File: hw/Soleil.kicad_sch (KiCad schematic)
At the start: 43 parts, among them J1 Conn_01x04, Q1 2N7002, SW1 SW_Push, U1 SPV1040TTR, U2 TPS61220DCK, U3 STM32G030F6Px, U4 ZJY200200-0154DAAMFGN

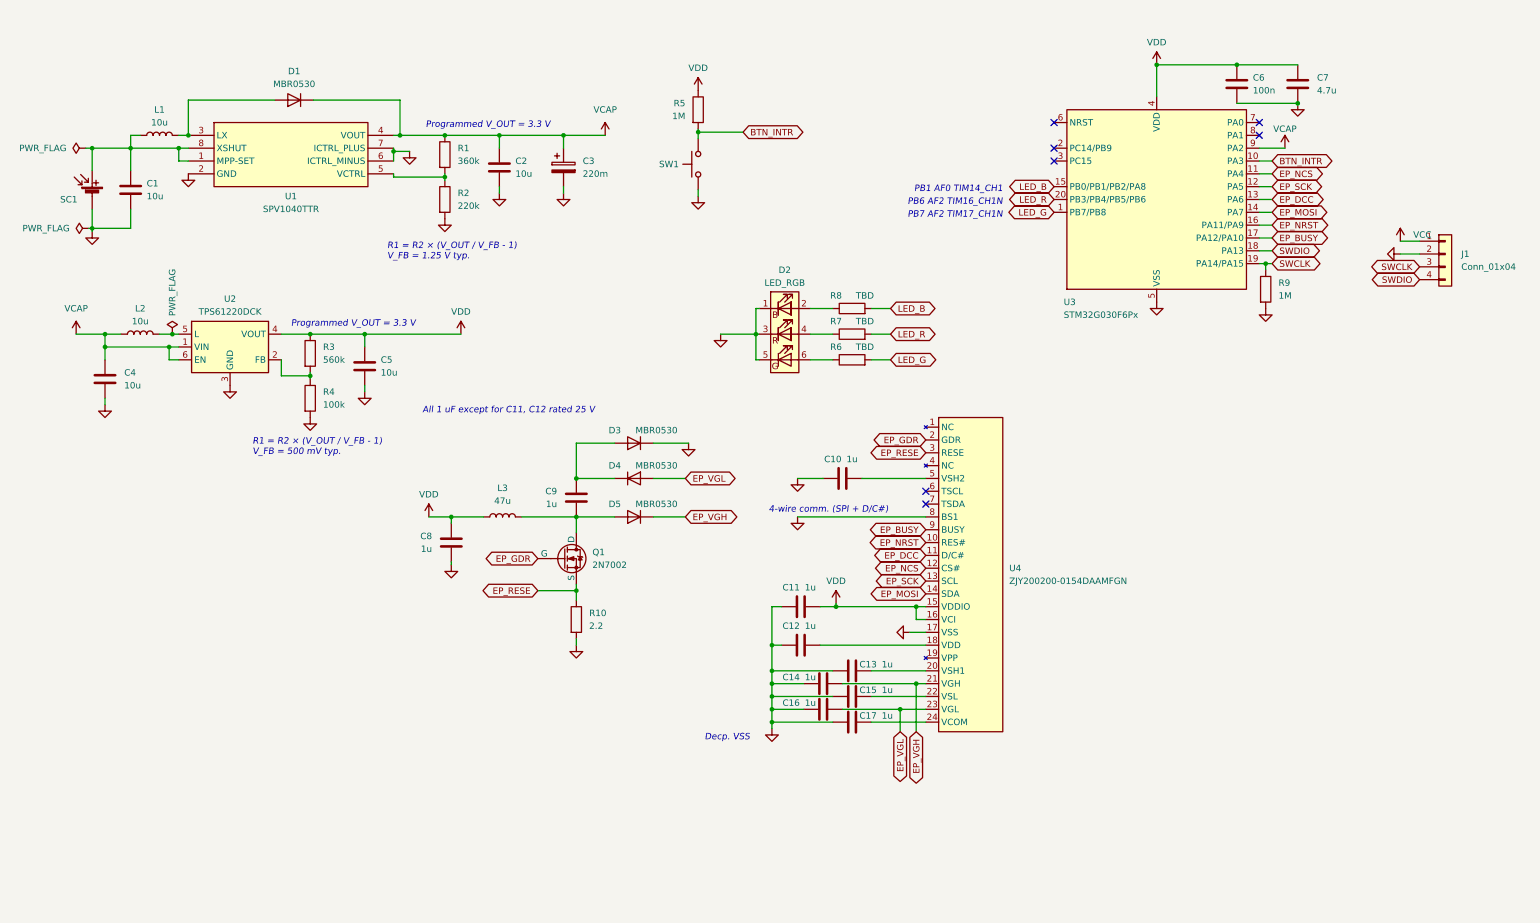
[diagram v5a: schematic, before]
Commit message: Update schematic to include analogue switch and flash
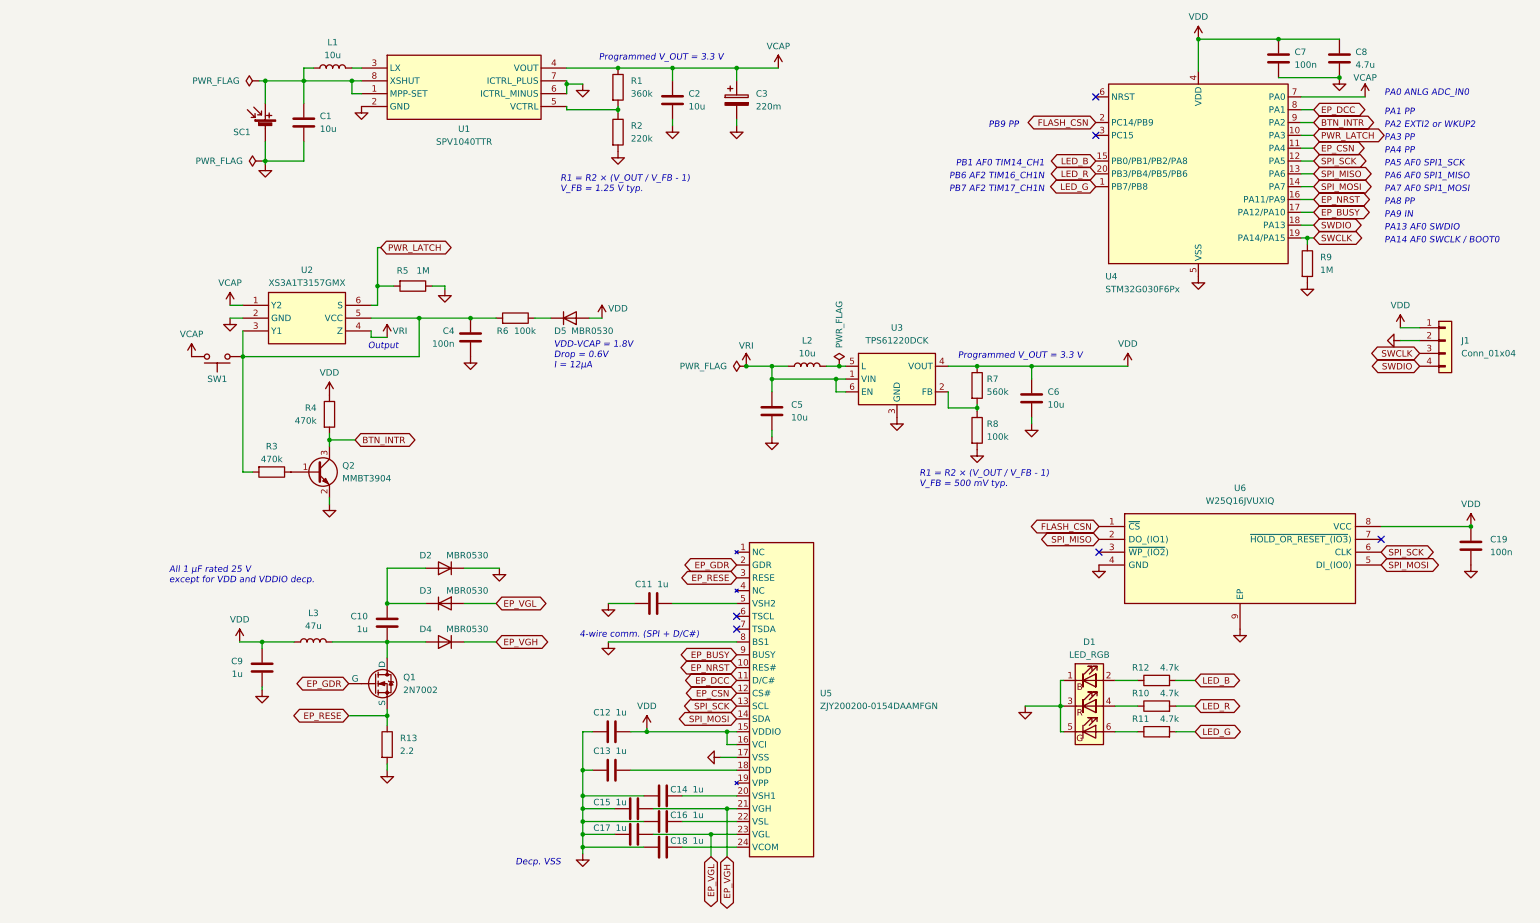
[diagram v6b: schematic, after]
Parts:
- removed D1: MBR0530, Diode_SMD:D_SOD-123, symbol Device:D
- added C19, C4: 100n, Capacitor_SMD:C_0603_1608Metric, symbol Device:C
- added D5: MBR0530, Diode_SMD:D_SOD-123, symbol Device:D
- added Q2: MMBT3904, Package_TO_SOT_SMD:SOT-23, symbol Transistor_BJT:MMBT3904
- added R3, R4: 470k, Resistor_SMD:R_0603_1608Metric, symbol Device:R
- added R6: 100k, Resistor_SMD:R_0603_1608Metric, symbol Device:R
- added U2: XS3A1T3157GMX, Soleil_footprints:XS3A1T3157GMX, symbol Soleil_symbols:XS3A1T3157GMX
- added U6: W25Q16JVUXIQ, Soleil_footprints:SON50P300X200X60-9N, symbol Soleil_symbols:W25Q16JVUXIQ
- R10: renamed from R7; value TBD -> 4.7k
- R11: renamed from R6; value TBD -> 4.7k
- R12: renamed from R8; value TBD -> 4.7k
- renumbered C9 to C10, C10 to C11, C11 to C12, C12 to C13, C13 to C14, C14 to C15, C15 to C16, C16 to C17, C17 to C18, C4 to C5, C5 to C6, C6 to C7, C7 to C8, C8 to C9, D2 to D1, D3 to D2, D4 to D3, D5 to D4, R10 to R13, R3 to R7, R4 to R8, U2 to U3, U3 to U4, U4 to U5
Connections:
- net BTN_INTR: now also U4.9 (PA2), Q2.3 (C), R4.2; no longer R5.2, SW1.1, U4.10 (PA3)
- net EP_DCC: now also U4.8 (PA1); no longer U4.13 (PA6)
- net GND: now also R5.1, C19.1, C4.1, Q2.2 (E), U2.2 (GND), U6.4 (GND), U6.9 (EP); no longer SW1.2
- net VCAP: now also SW1.1, U4.7 (PA0), U2.1 (Y2); no longer C5.1, L2.1, U3.1 (VIN), U3.6 (EN), U4.9 (PA2)
- net VDD: now also C19.2, D5.2 (A), R4.1, U6.8 (VCC); no longer R5.1
- net FLASH_CSN: now reaches U4.2 (PC14/PB9)
- net FLASH_CSN: now also U6.1 (~{CS})
- net EP_MOSI renamed SPI_MOSI
- net SPI_MOSI: now also U6.5 (DI_(IO0))
- net EP_NCS renamed EP_CSN
- net EP_SCK renamed SPI_SCK
- net SPI_SCK: now also U6.6 (CLK)
- new net: Q2.1 (B), R3.1
- new net: C4.2, R3.2, R6.2, SW1.2, U2.3 (Y1), U2.5 (VCC)
- new net: D5.1 (K), R6.1
- new net PWR_LATCH: R5.2, U2.6 (S), U4.10 (PA3)
- new net SPI_MISO: U4.13 (PA6), U6.2 (DO_(IO1))
- new net VRI: C5.1, L2.1, U2.4 (Z), U3.1 (VIN), U3.6 (EN)
- no-connect marks 7 -> 6
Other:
- note added: "All 1 µF rated 25 V except for VDD and VDDIO decp."
- note added: "Output"
- note added: "PA0 ANLG ADC_IN0"
- note added: "PA1 PP"
- note added: "PA13 AF0 SWDIO"
- note added: "PA14 AF0 SWCLK / BOOT0"
- note added: "PA2 EXTI2 or WKUP2"
- note added: "PA3 PP"
- note added: "PA4 PP"
- note added: "PA5 AF0 SPI1_SCK"
- note added: "PA6 AF0 SPI1_MISO"
- note added: "PA7 AF0 SPI1_MOSI"
- note added: "PA8 PP"
- note added: "PA9 IN"
- note added: "PB9 PP"
- note added: "VDD-VCAP = 1.8V Drop = 0.6V I = 12µA"
- note removed: "All 1 uF except for C11, C12 rated 25 V"
- moved on the sheet: C1, C10, C11, C12, C13, C14, C15, C16, C17, C18, C2, C3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

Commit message: Revise and simplify schematic
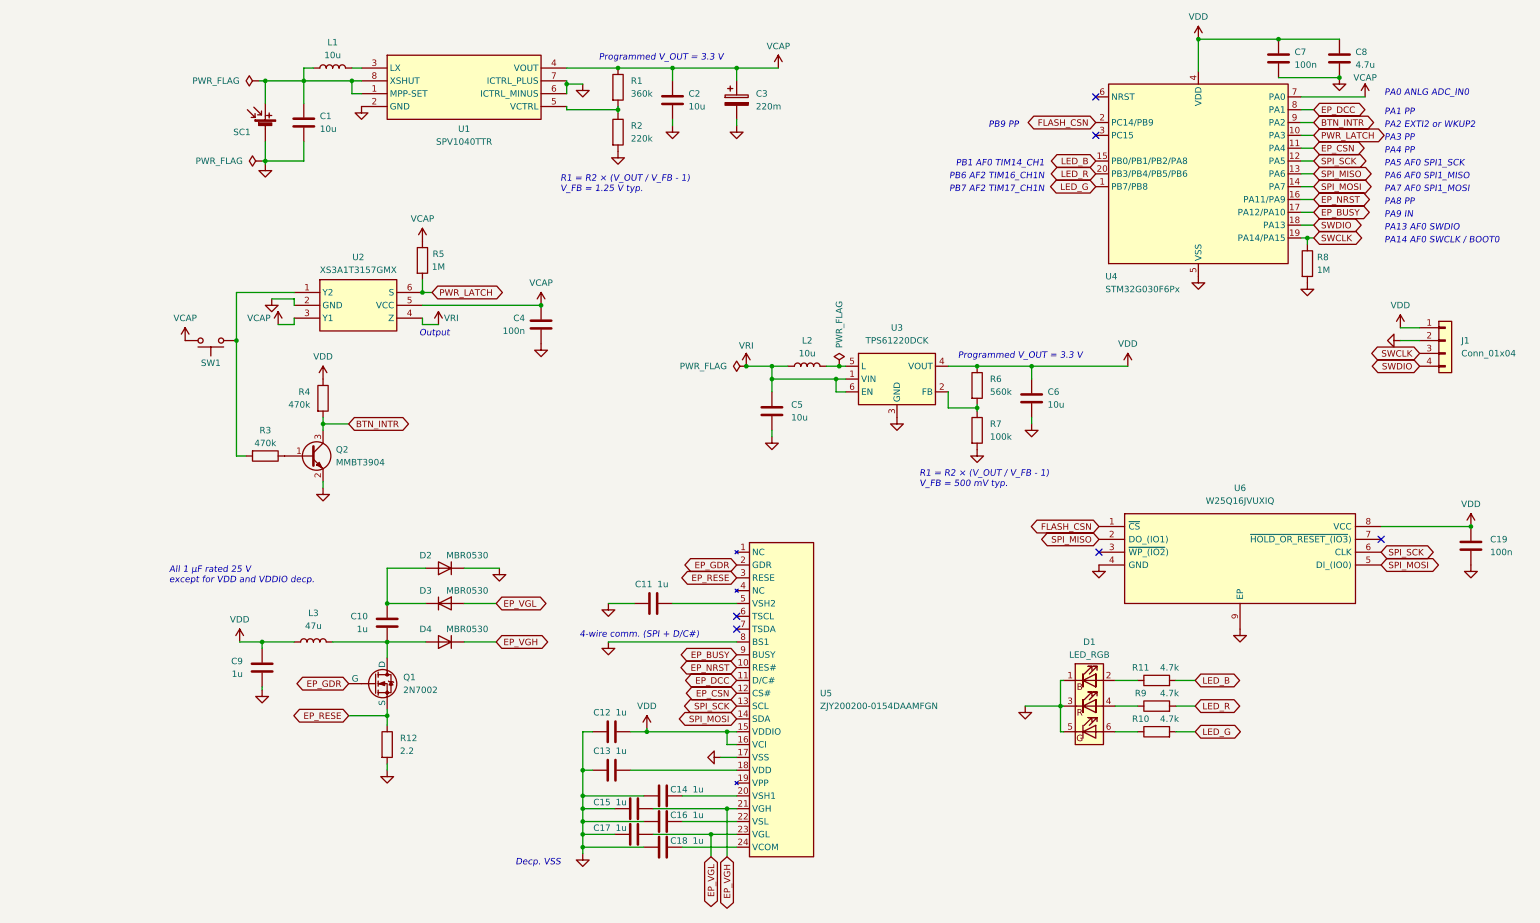
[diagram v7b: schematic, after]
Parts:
- removed D5: MBR0530, Diode_SMD:D_SOD-123, symbol Device:D
- removed R6: 100k, Resistor_SMD:R_0603_1608Metric, symbol Device:R
- renumbered R11 to R10, R12 to R11, R13 to R12, R7 to R6, R8 to R7, R9 to R8, R10 to R9
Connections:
- net GND: no longer R5.1
- net VCAP: now also C4.2, R5.1, U2.3 (Y1), U2.5 (VCC); no longer U2.1 (Y2)
- new net: R3.2, SW1.2, U2.1 (Y2)
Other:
- note removed: "VDD-VCAP = 1.8V Drop = 0.6V I = 12µA"
- moved on the sheet: C4, Q2, R3, R4, R5, SW1, U2

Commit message: Revise board design; submit for fab (Rev. 5)
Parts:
- renumbered Q2 to Q1, Q1 to Q2
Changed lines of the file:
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@@
   )
   (symbol (lib_id "Device:Q_NMOS_GSD") (at 55.88 147.955 0) (unit 1)
-    (in_bom yes) (on_board yes) (dnp no) (fields_autoplaced)
-    (property "Reference" "Q1" (at 61.595 146.685 0)
+    (in_bom yes) (on_board yes) (dnp no)
+    (property "Reference" "Q2" (at 61.595 146.685 0)
       (effects (font (size 1.27 1.27)) (justify left))
     )
@@
       (project "Soleil"
         (path "/218ebbfa-f714-4191-a352-4c256789be77"
-          (reference "Q1") (unit 1)
+          (reference "Q2") (unit 1)
         )
       )
@@
   (symbol (lib_id "Transistor_BJT:MMBT3904") (at 43.18 102.87 0) (unit 1)
     (in_bom yes) (on_board yes) (dnp no) (fields_autoplaced)
-    (property "Reference" "Q2" (at 48.26 101.6 0)
+    (property "Reference" "Q1" (at 48.26 101.6 0)
       (effects (font (size 1.27 1.27)) (justify left))
     )
@@
       (project "Soleil"
         (path "/218ebbfa-f714-4191-a352-4c256789be77"
-          (reference "Q2") (unit 1)
-        )
-      )
+          (reference "Q1") (unit 1)
+        )
+      )
